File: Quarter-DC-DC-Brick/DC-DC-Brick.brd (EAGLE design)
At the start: 50.8 x 76.2 mm, 20 parts

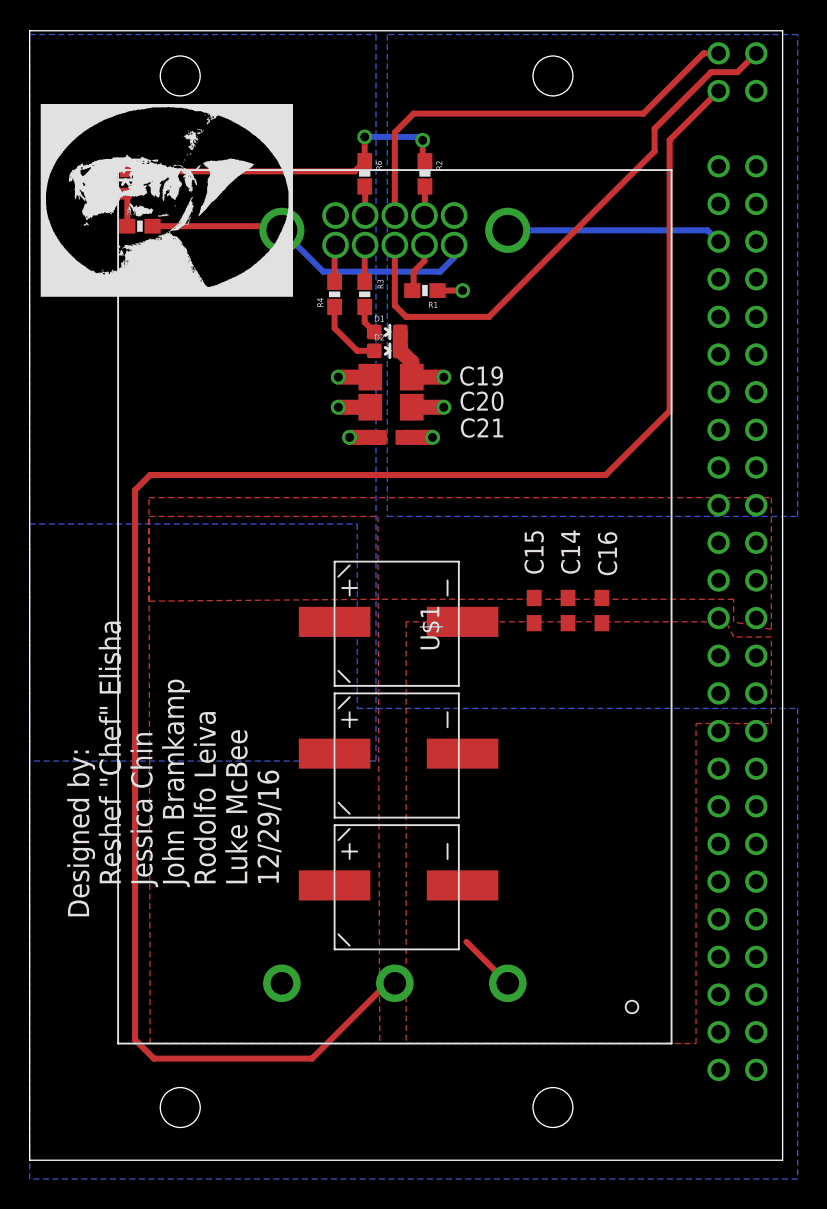
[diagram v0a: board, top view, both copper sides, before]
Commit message: Created new board for quarter brick
made new board for quarter brick to be used
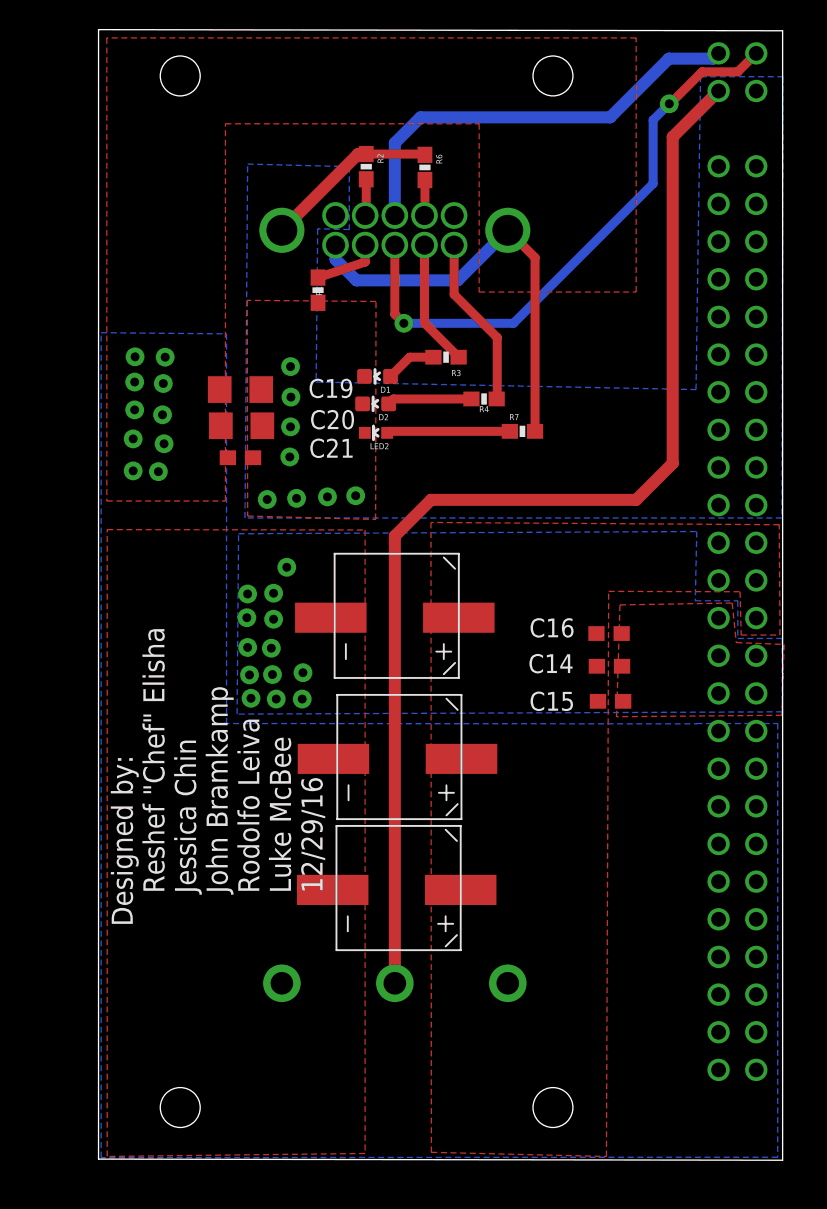
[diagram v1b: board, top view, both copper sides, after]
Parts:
- moved R7 29.3 mm to (33.2, 49.2)
- moved LED2 23.9 mm to (23.4, 49.1), turned to 90 degrees
- moved R4 12.3 mm to (30.7, 51.4), turned to 0 degrees
- moved C22V1 12.2 mm to (20.6, 40.9), turned to 270 degrees
- moved C22V6 11.7 mm to (20.7, 22.6), turned to 270 degrees
- moved C22V5 11.7 mm to (20.8, 31.4), turned to 270 degrees
- moved C21 10.3 mm to (14.2, 47.4)
- moved C19 10.2 mm to (14.2, 52.0)
- moved C20 10.2 mm to (14.3, 49.6)
- moved C15 8.00 mm to (39.2, 31.0), turned to 0 degrees
- moved R1 7.21 mm to (19.5, 58.7), turned to 90 degrees
- moved R3 6.93 mm to (28.1, 54.2), turned to 0 degrees
- moved C14 4.68 mm to (39.1, 33.3), turned to 0 degrees
- moved R6 4.09 mm to (26.7, 67.0)
- moved R2 3.99 mm to (22.7, 67.0)
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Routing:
- net ON/OFF: track 118.5 -> 77.4 mm
- net GND: track 49.4 -> 11.8 mm, vias 6 -> 8
- net N$6: track 2.49 -> 11.6 mm
- net N$7: track 2.48 -> 8.51 mm
- net N$12: track 2.31 -> 8.32 mm
- net V-: track 3.95 -> 0.00 mm, vias 0 -> 13
- net N$10: track 37.0 -> 39.4 mm, vias 0 -> 2
- net N$4: track 1.96 -> 3.43 mm
- net N$2: track 3.40 -> 4.49 mm
- net N$5: track 4.75 -> 5.72 mm
- net V+: track 29.4 -> 28.9 mm, vias 3 -> 10
- added copper zone on layer 1, net GND
- added copper zone on layer 1, net V+
- added copper zone on layer 16, net V-
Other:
- board size 50.8 x 76.2 mm -> 46.2 x 76.3 mm

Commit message: redesigned 1/4 brick board
redesigned quarter brick (and 1/8th brick) board
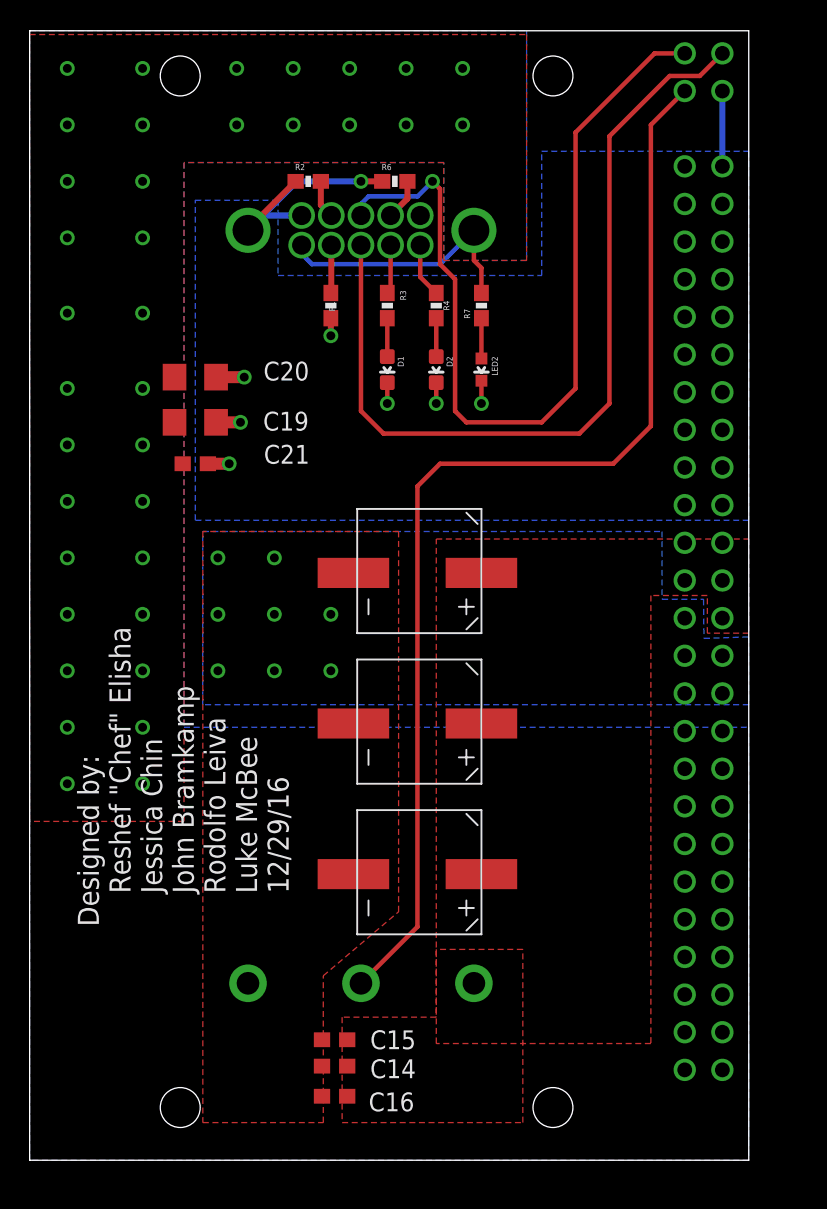
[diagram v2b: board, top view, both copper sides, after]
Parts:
- moved C16 36.3 mm to (20.6, 4.32), turned to 180 degrees
- moved C14 32.7 mm to (20.6, 6.35), turned to 180 degrees
- moved C15 29.5 mm to (20.6, 8.13), turned to 180 degrees
- moved R7 8.92 mm to (30.5, 57.7), turned to 90 degrees
- moved LED2 8.29 mm to (30.5, 53.3), turned to 180 degrees
- moved R4 7.08 mm to (27.4, 57.7), turned to 90 degrees
- moved R3 5.27 mm to (24.1, 57.7), turned to 90 degrees
- moved D2 4.70 mm to (27.4, 53.3), turned to 180 degrees
- moved C20 4.53 mm to (11.2, 52.8)
- moved R2 4.04 mm to (18.8, 66.0), turned to 0 degrees
- moved C19 3.76 mm to (11.2, 49.8)
- moved C22V1 3.39 mm to (22.1, 43.9)
- moved C21 3.07 mm to (11.2, 47.0)
- moved C22V5 2.74 mm to (22.1, 33.8)
- moved U$1 2.29 mm to (22.4, 37.3)
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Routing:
- net N$8: track 29.2 -> 58.6 mm, vias 0 -> 1
- net GND: track 11.8 -> 34.7 mm
- net N$10: track 39.4 -> 57.4 mm, vias 2 -> 0
- net V+: track 28.9 -> 17.9 mm, vias 10 -> 36
- net N$6: track 11.6 -> 3.68 mm
- net N$12: track 8.32 -> 2.72 mm
- net N$7: track 8.51 -> 3.32 mm
- net N$5: track 5.72 -> 2.59 mm
- net ON/OFF: track 77.4 -> 76.1 mm
- net N$2: track 4.49 -> 3.24 mm
- net N$4: track 3.43 -> 2.59 mm
- removed copper zone on layer 1, net GND
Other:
- board size 46.2 x 76.3 mm -> 48.5 x 76.2 mm
